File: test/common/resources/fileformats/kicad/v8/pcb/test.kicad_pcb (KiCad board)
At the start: 2 copper layers, 4 parts

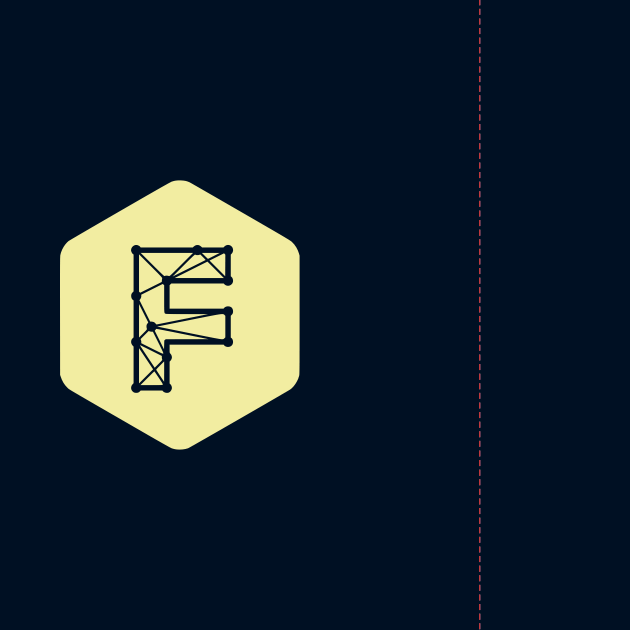
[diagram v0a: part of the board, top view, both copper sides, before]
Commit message: switch to lazy registration of unit types in typegraph
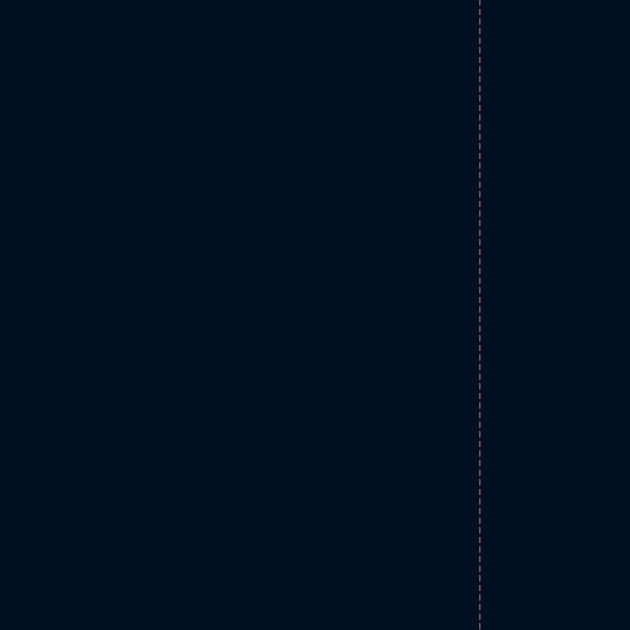
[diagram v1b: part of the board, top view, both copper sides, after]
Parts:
- G***: moved to B.Cu
- moved G*** 22.4 mm to (20.0, 40.0), turned to 90 degrees

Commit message: reset test file
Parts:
- G***: moved to F.Cu
- moved G*** 22.4 mm to (10.0, 20.0), turned to 0 degrees

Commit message: fast without cacheing
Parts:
- G***: moved to B.Cu
- turned G*** to 90 degrees

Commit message: revert node to main, fix all .is_unit references on unit instances
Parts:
- moved G*** 156.5 mm to (80.0, 160.0), turned to 0 degrees
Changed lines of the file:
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@@
 	(footprint "logos:faebryk_logo"
 		(layer "B.Cu")
-		(at 10 20 90)
+		(at 80 160)
 		(property "Reference" "G***"
-			(at 0 -0 270)
+			(at 0 -0 180)
 			(layer "B.SilkS")
 			(hide yes)
@@
 		)
 		(property "Value" "LOGO"
-			(at 0.75 -0 270)
+			(at 0.75 -0 180)
 			(layer "B.SilkS")
 			(hide yes)
@@
 		)
 		(property "Footprint" "logos:faebryk_logo"
-			(at 0 -0 270)
+			(at 0 -0 180)
 			(layer "B.Fab")
 			(hide no)
@@
 		)
 		(property "Datasheet" ""
-			(at 0 -0 270)
+			(at 0 -0 180)
 			(layer "B.Fab")
 			(hide yes)
@@
 		)
 		(property "Description" ""
-			(at 0 -0 270)
+			(at 0 -0 180)
 			(layer "B.Fab")
 			(hide yes)

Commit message: bug fix
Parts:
- G***: moved to F.Cu
- moved G*** 22.4 mm to (90.0, 180.0), turned to 90 degrees

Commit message: pytest fixes
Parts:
- moved G*** 67.1 mm to (120.0, 240.0), turned to 180 degrees
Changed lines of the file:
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@@
 	(footprint "logos:faebryk_logo"
 		(layer "F.Cu")
-		(at 90 180 90)
+		(at 120 240 180)
 		(property "Reference" "G***"
-			(at 0 0 270)
+			(at 0 0 180)
 			(layer "F.SilkS")
 			(hide yes)
@@
 		)
 		(property "Value" "LOGO"
-			(at 0.75 0 270)
+			(at 0.75 0 180)
 			(layer "F.SilkS")
 			(hide yes)
@@
 		)
 		(property "Footprint" "logos:faebryk_logo"
-			(at 0 0 270)
+			(at 0 0 180)
 			(layer "F.Fab")
 			(hide no)
@@
 		)
 		(property "Datasheet" ""
-			(at 0 0 270)
+			(at 0 0 180)
 			(layer "F.Fab")
 			(hide yes)
@@
 		)
 		(property "Description" ""
-			(at 0 0 270)
+			(at 0 0 180)
 			(layer "F.Fab")
 			(hide yes)

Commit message: more pytest fix
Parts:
- moved G*** 246.0 mm to (10.0, 20.0), turned to 0 degrees
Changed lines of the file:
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@@
 	(footprint "logos:faebryk_logo"
 		(layer "F.Cu")
-		(at 120 240 180)
+		(at 10 20 0)
 		(property "Reference" "G***"
-			(at 0 0 180)
+			(at 0 0 0)
 			(layer "F.SilkS")
 			(hide yes)
@@
 		)
 		(property "Value" "LOGO"
-			(at 0.75 0 180)
+			(at 0.75 0 0)
 			(layer "F.SilkS")
 			(hide yes)
@@
 		)
 		(property "Footprint" "logos:faebryk_logo"
-			(at 0 0 180)
+			(at 0 0 0)
 			(layer "F.Fab")
 			(hide no)
@@
 					(thickness 0.15)
 				)
-				(justify right mirror)
+				(justify mirror right)
 			)
 		)
 		(property "Datasheet" ""
-			(at 0 0 180)
+			(at 0 0 0)
 			(layer "F.Fab")
 			(hide yes)
@@
 		)
 		(property "Description" ""
-			(at 0 0 180)
+			(at 0 0 0)
 			(layer "F.Fab")
 			(hide yes)
